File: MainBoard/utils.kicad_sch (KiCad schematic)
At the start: 16 parts, among them U3 LIS3DH, U4 AT42QT1011-TSHR

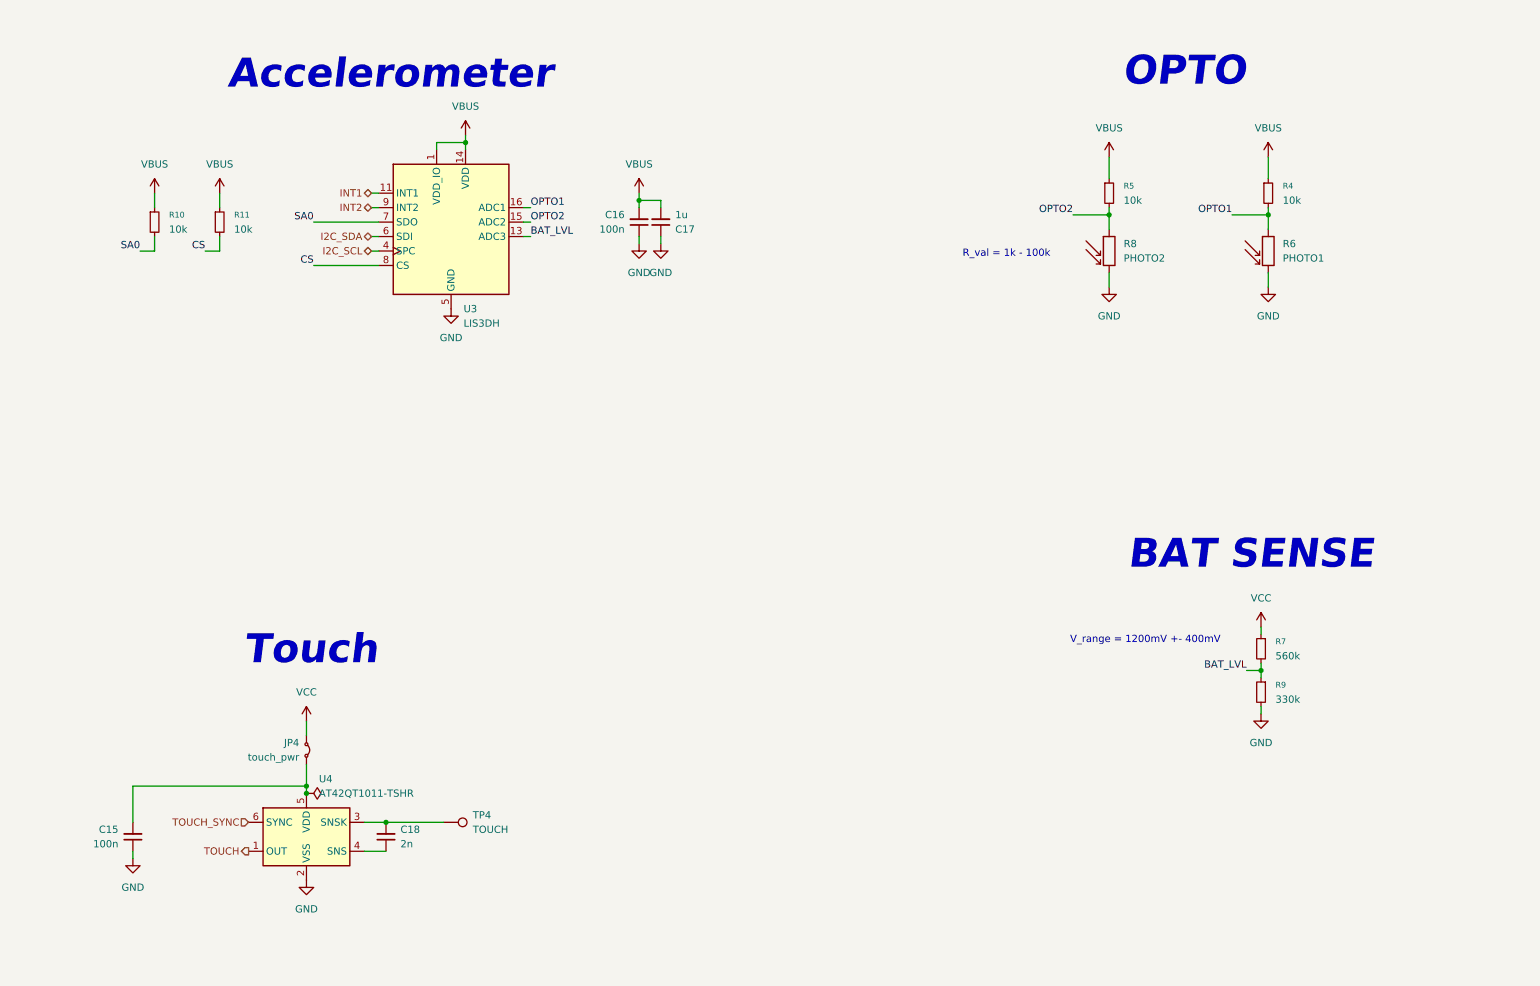
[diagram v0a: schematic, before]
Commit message: change schematic, use touch controller to enable second bard power. microcontroller should set pin up to latch power
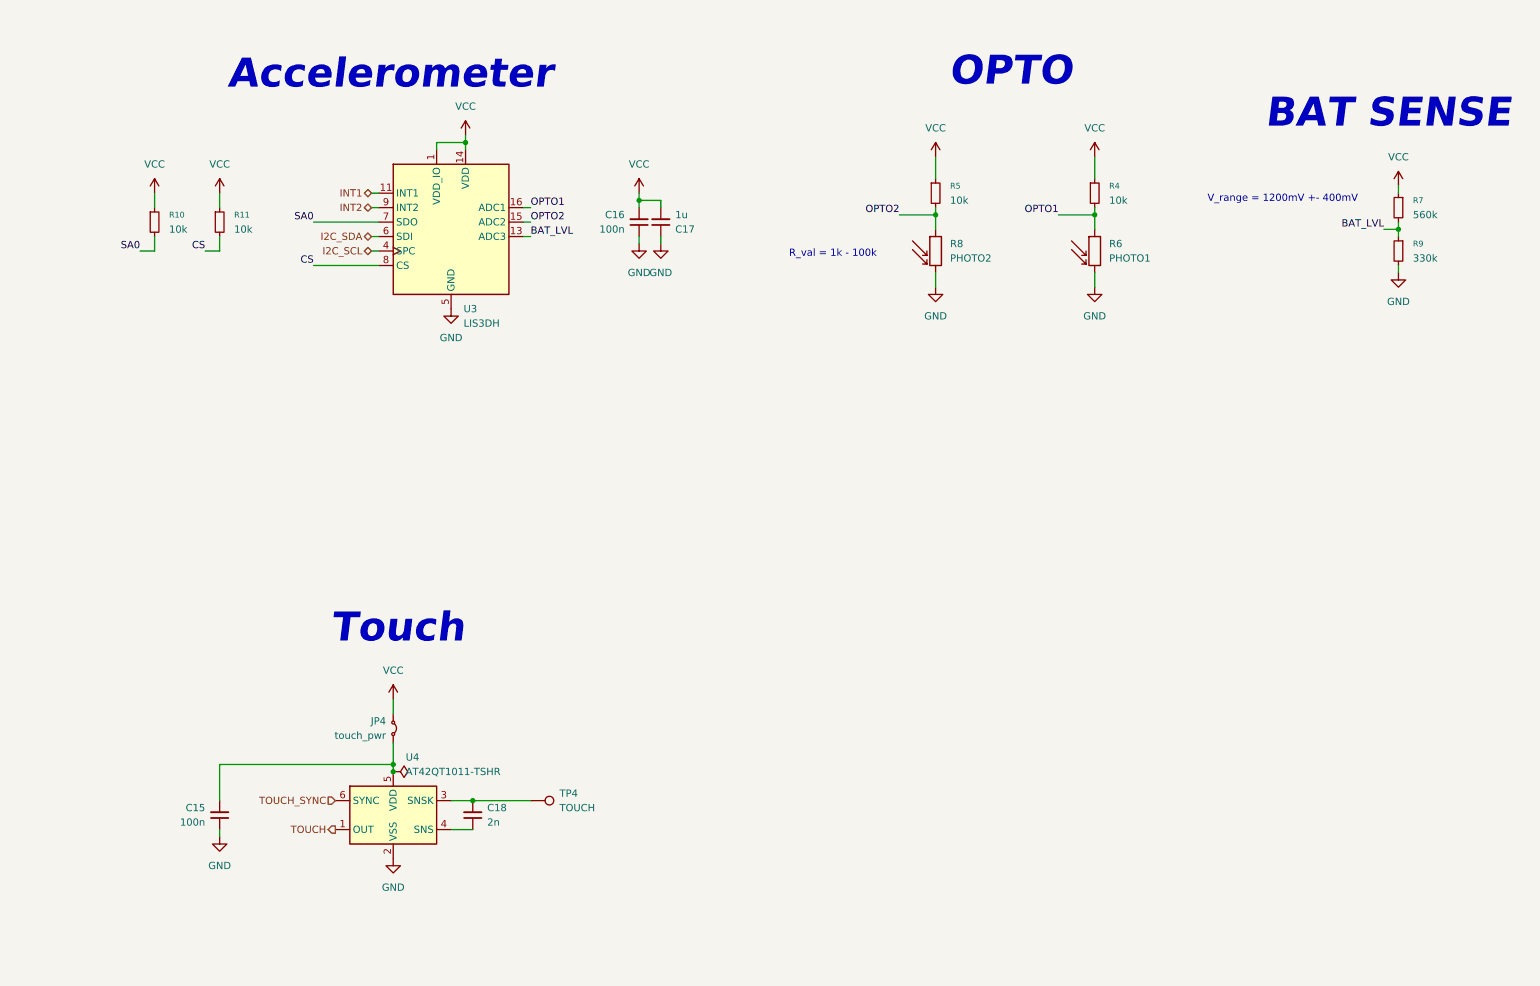
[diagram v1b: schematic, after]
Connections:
- net VBUS is gone; now on net VCC: C16.2, C17.2, R10.1, R11.1, R4.1, R5.1, U3.1 (VDD_IO), U3.14 (VDD)
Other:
- moved on the sheet: C15, C18, JP4, R4, R5, R6, R7, R8, R9, TP4, U4

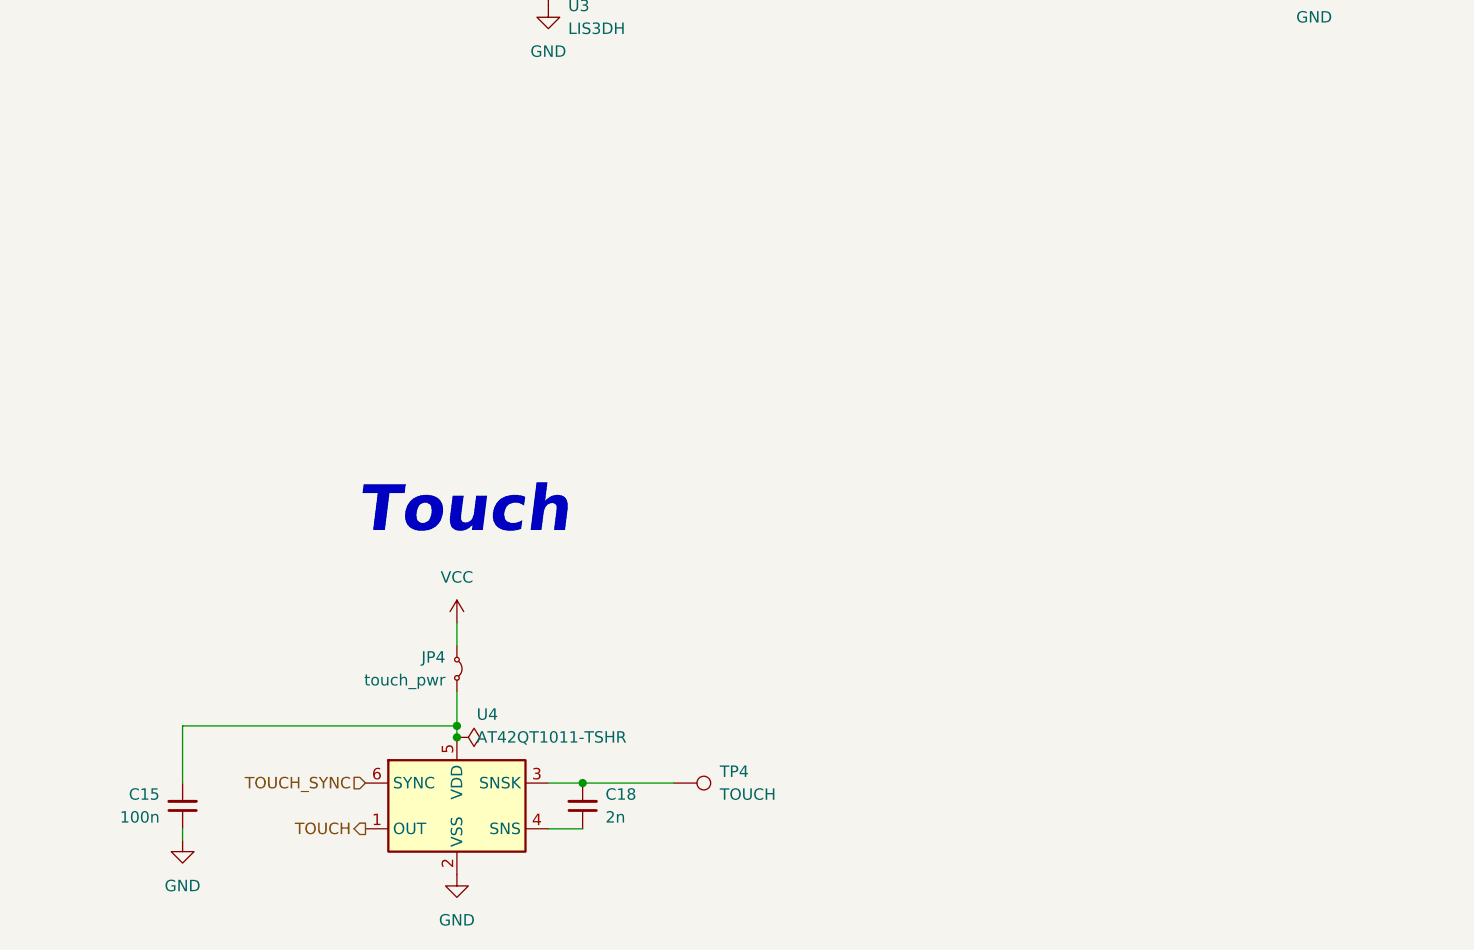
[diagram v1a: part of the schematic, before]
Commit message: Change location of tuch sensor, touch button now power up all components, change length. Add buzzer to mainboard and remove touch from them. change revision version
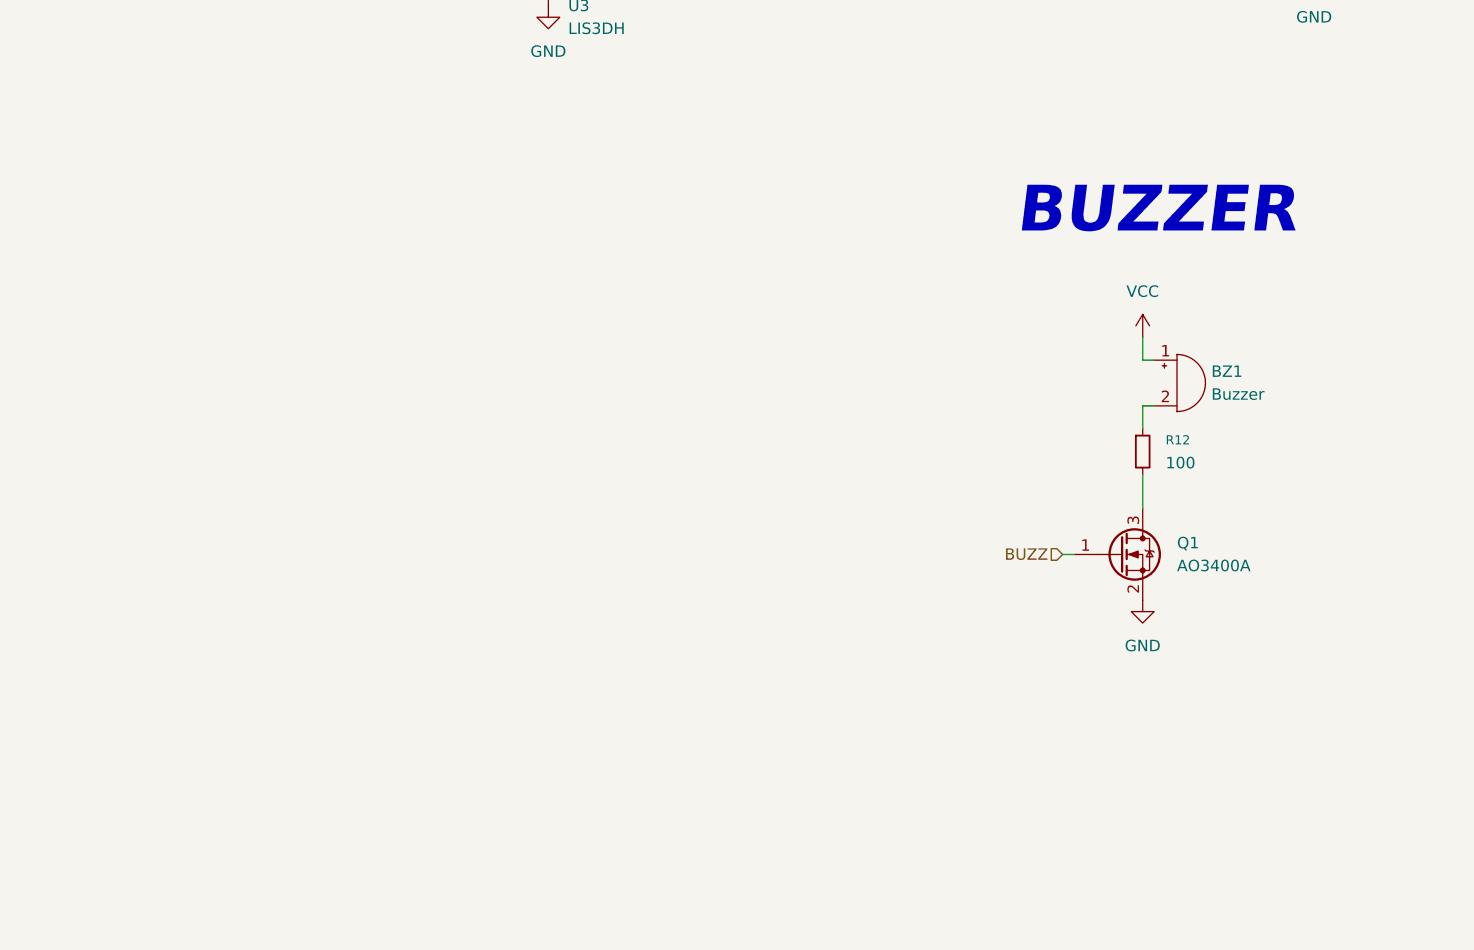
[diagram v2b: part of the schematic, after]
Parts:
- removed C15: 100n, Capacitor_SMD:C_0603_1608Metric_Pad1.08x0.95mm_HandSolder, symbol Device:C_Small
- removed C18: 2n, Capacitor_SMD:C_0603_1608Metric_Pad1.08x0.95mm_HandSolder, symbol Device:C_Small
- removed JP4: touch_pwr, Jumper:SolderJumper-2_P1.3mm_Bridged2Bar_RoundedPad1.0x1.5mm, symbol Jumper:Jumper_2_Small_Bridged
- removed TP4: TOUCH, TestPoint:TestPoint_Pad_D3.0mm, symbol Connector:TestPoint
- removed U4: AT42QT1011-TSHR, Package_TO_SOT_SMD:SOT-23-6, symbol Sensor_Touch:AT42QT1011-TSHR
- added BZ1: Buzzer, Buzzer_Beeper:Buzzer_Murata_PKMCS0909E, symbol Device:Buzzer
- added Q1: AO3400A, Package_TO_SOT_SMD:SOT-23, symbol Transistor_FET:AO3400A
- added R12: 100, Resistor_SMD:R_0603_1608Metric_Pad0.98x0.95mm_HandSolder, symbol Device:R_Small
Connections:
- net GND: now also Q1.2 (S)
- net VCC: now also BZ1.1 (+)
- new net: BZ1.2 (-), R12.1
- new net: Q1.3 (D), R12.2
- new net BUZZ: Q1.1 (G)
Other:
- note added: "BUZZER"
- note removed: "Touch"

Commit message: add buzer, update layout to schematic, make pcb mounting
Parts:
- BZ1: footprint Buzzer_Beeper:Buzzer_Murata_PKMCS0909E -> buzzer:Buzzer_SMD_5020
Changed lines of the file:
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@@
 			)
 		)
-		(property "Footprint" "Buzzer_Beeper:Buzzer_Murata_PKMCS0909E"
+		(property "Footprint" "buzzer:Buzzer_SMD_5020"
 			(at 160.655 111.76 90)
 			(effects

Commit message: change schematic
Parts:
- added J1: touch plate, Connector_Pin:Pin_D1.0mm_L10.0mm, symbol Connector:Conn_01x01_Pin
- added J2: Matrix_in, Connector_PinSocket_2.54mm:PinSocket_1x03_P2.54mm_Vertical, symbol Connector:Conn_01x03_Socket
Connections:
- net GND: now also J2.2 (Pin_2)
- net VCC: now also J2.1 (Pin_1)
- new net DATA_MATRIX: J2.3 (Pin_3)
- new net TOUCH: J1.1 (Pin_1)
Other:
- note added: "Matrix out"
- note added: "TOUCH"
- moved on the sheet: BZ1, C16, C17, Q1, R10, R11, R12, R4, R5, R6, R7, R8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

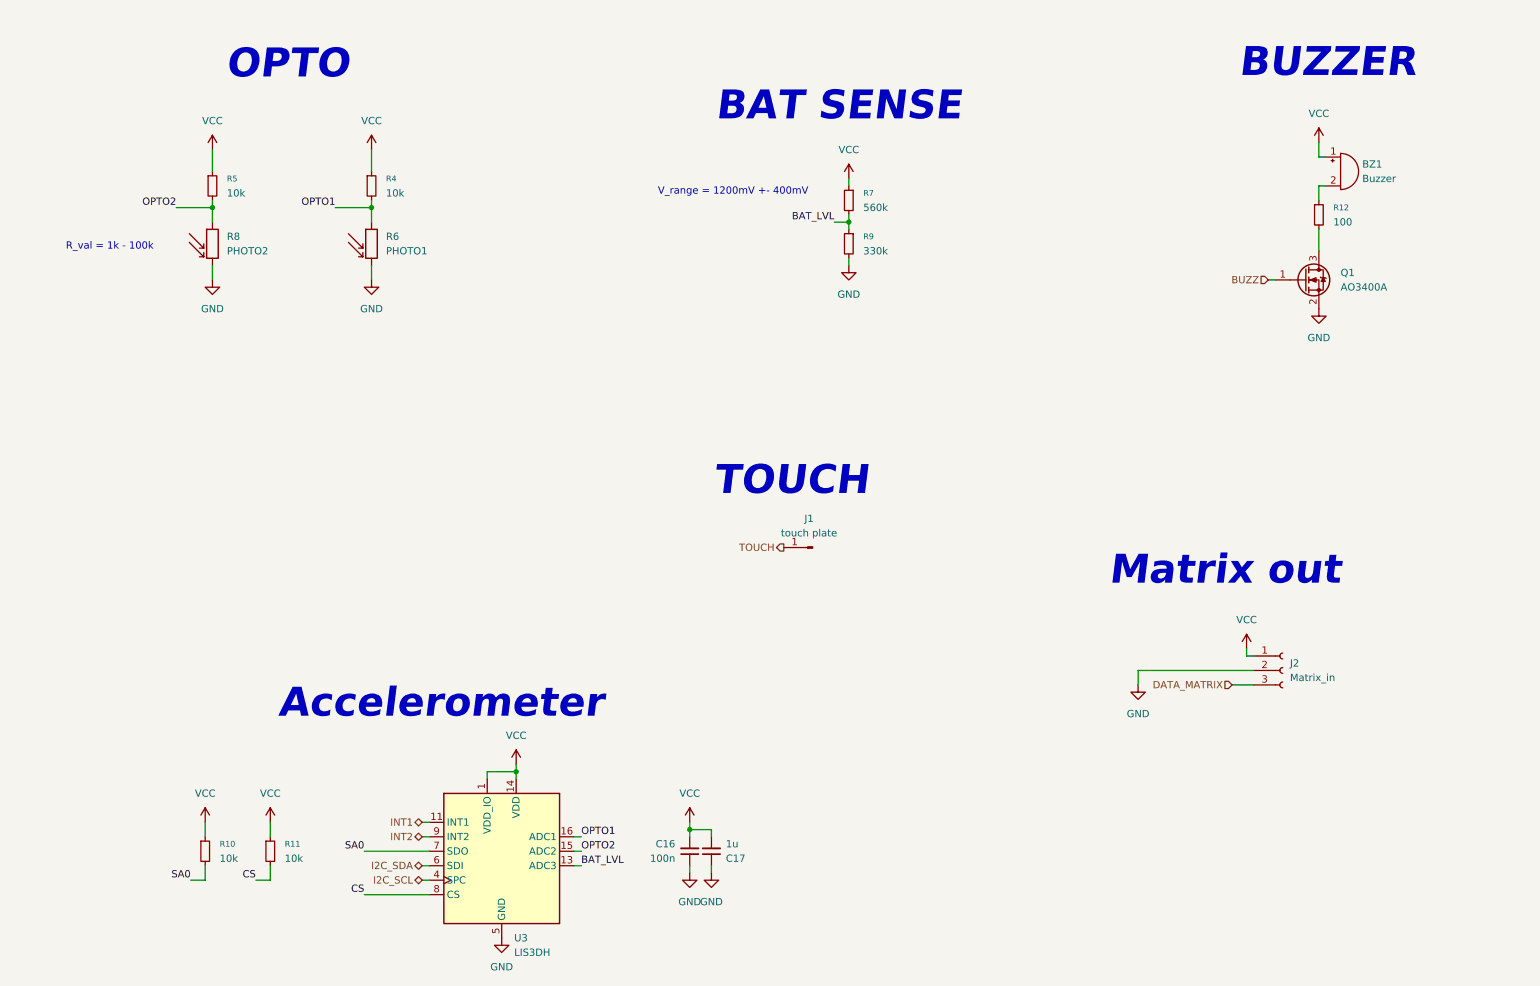
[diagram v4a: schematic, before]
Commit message: Change project assumptions, create new board with esp32-c3
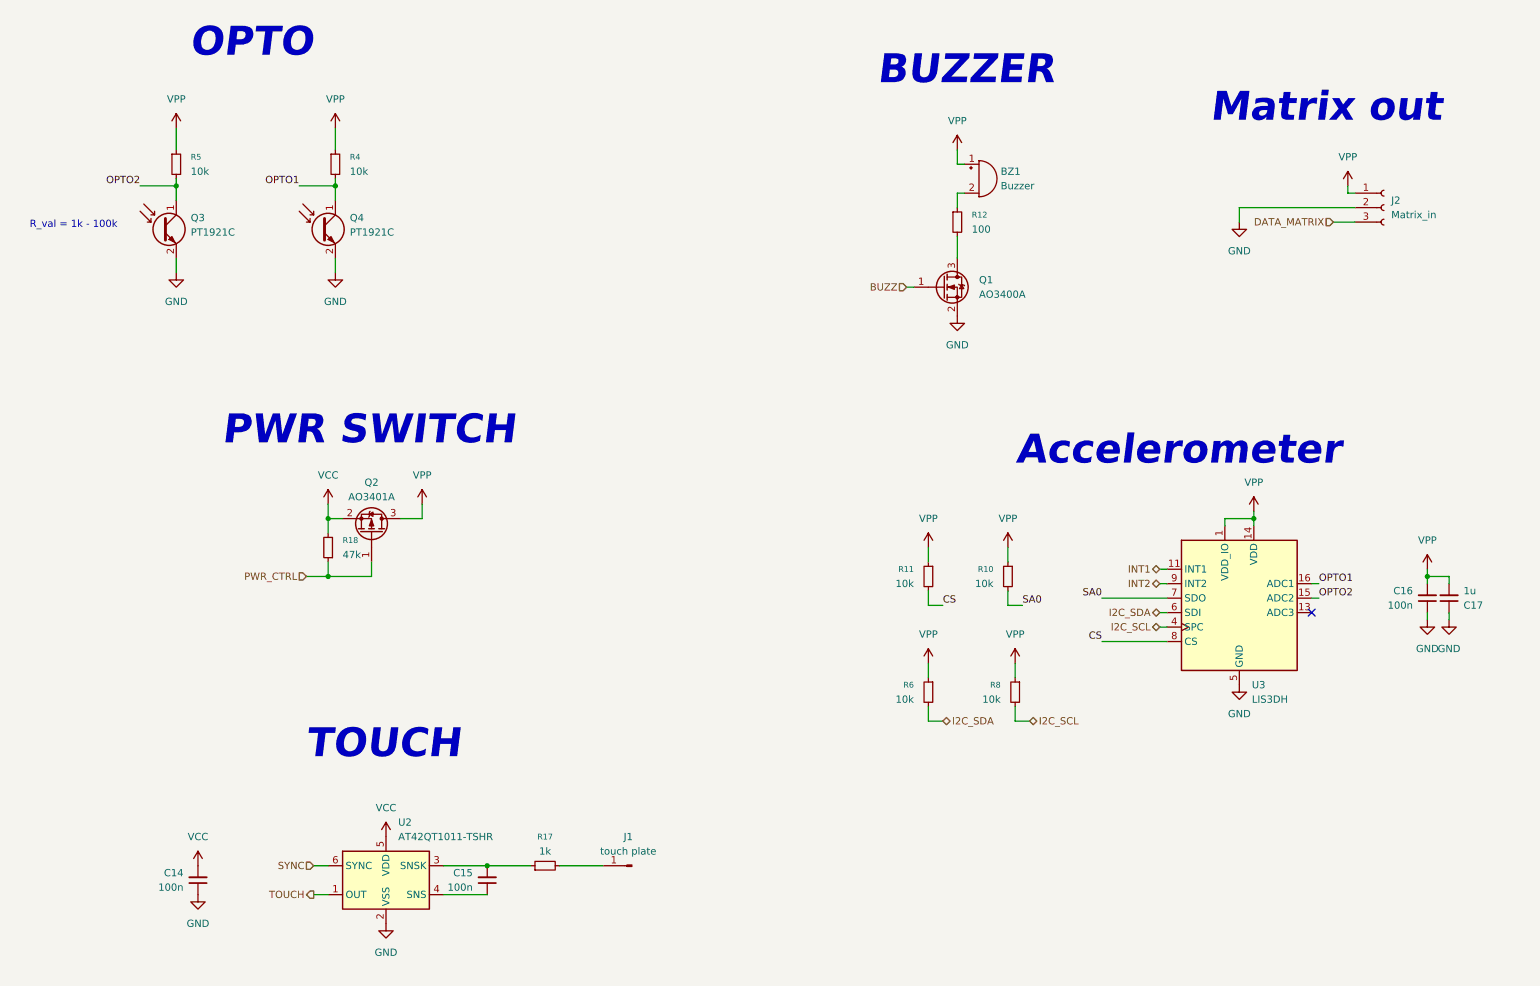
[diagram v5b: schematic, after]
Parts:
- removed R6: PHOTO1, OptoDevice:Osram_LPT80A, symbol Device:R_Photo
- removed R7: 560k, Resistor_SMD:R_0603_1608Metric_Pad0.98x0.95mm_HandSolder, symbol Device:R_Small
- removed R8: PHOTO2, OptoDevice:Osram_LPT80A, symbol Device:R_Photo
- removed R9: 330k, Resistor_SMD:R_0603_1608Metric_Pad0.98x0.95mm_HandSolder, symbol Device:R_Small
- added C14, C15: 100n, Capacitor_SMD:C_0603_1608Metric_Pad1.08x0.95mm_HandSolder, symbol Device:C_Small
- added Q2: AO3401A, Package_TO_SOT_SMD:SOT-23, symbol Transistor_FET:AO3401A
- added Q3, Q4: PT1921C, Diode_SMD:D_0603_1608Metric_Pad1.05x0.95mm_HandSolder, symbol Device:Q_Photo_NPN
- added R17: 1k, Resistor_SMD:R_0603_1608Metric_Pad0.98x0.95mm_HandSolder, symbol Device:R_Small
- added R18: 47k, Resistor_SMD:R_0603_1608Metric_Pad0.98x0.95mm_HandSolder, symbol Device:R_Small
- added R6, R8: 10k, Resistor_SMD:R_0603_1608Metric_Pad0.98x0.95mm_HandSolder, symbol Device:R_Small
- added U2: AT42QT1011-TSHR, Package_TO_SOT_SMD:SOT-23-6, symbol Sensor_Touch:AT42QT1011-TSHR
- J1: footprint Connector_Pin:Pin_D1.0mm_L10.0mm -> touch:FW-UU_05_11_28
- J2: footprint Connector_PinSocket_2.54mm:PinSocket_1x03_P2.54mm_Vertical -> Connector_JST:JST_PH_B3B-PH-K_1x03_P2.00mm_Vertical
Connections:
- net GND: now also C14.1, Q3.2 (E), Q4.2 (E), U2.2 (VSS)
- net I2C_SCL: now also R8.2
- net I2C_SDA: now also R6.2
- net OPTO1: now also Q4.1 (C)
- net OPTO2: now also Q3.1 (C)
- net TOUCH: now also U2.1 (OUT); no longer J1.1 (Pin_1)
- net VCC: now also C14.2, Q2.2 (S), R18.2, U2.5 (VDD); no longer BZ1.1 (+), C16.2, C17.2, J2.1 (Pin_1), R10.1, R11.1, R4.1, R5.1, U3.1 (VDD_IO), U3.14 (VDD)
- net BAT_LVL: no longer names the net of U3.13 (ADC3)
- new net: C15.1, U2.4 (SNS)
- new net: C15.2, R17.1, U2.3 (SNSK)
- new net: J1.1 (Pin_1), R17.2
- new net PWR_CTRL: Q2.1 (G), R18.1
- new net SYNC: U2.6 (SYNC)
- new net VPP: BZ1.1 (+), C16.2, C17.2, J2.1 (Pin_1), Q2.3 (D), R10.1, R11.1, R4.1, R5.1, R6.1, R8.1, U3.1 (VDD_IO), U3.14 (VDD)
- no-connect marks 0 -> 1
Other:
- note added: "PWR SWITCH"
- note removed: "BAT SENSE"
- note removed: "V_range = 1200mV +- 400mV"
- moved on the sheet: BZ1, C16, C17, J1, J2, Q1, R10, R11, R12, R4, R5, U3
